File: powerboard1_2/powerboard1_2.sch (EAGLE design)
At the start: 118 parts, among them Q1 IPP80P03P4L04AKSA1, Q2 2N4401TFR, Q3 2N4401TFR, Q4 2N4401TFR, T1 2_POS_TERMINAL, U1 UWE-12/10-Q12PB-C, U2 UWE-5/15-Q12PB-C, U3 UWE-3.3/20-Q12PB-C

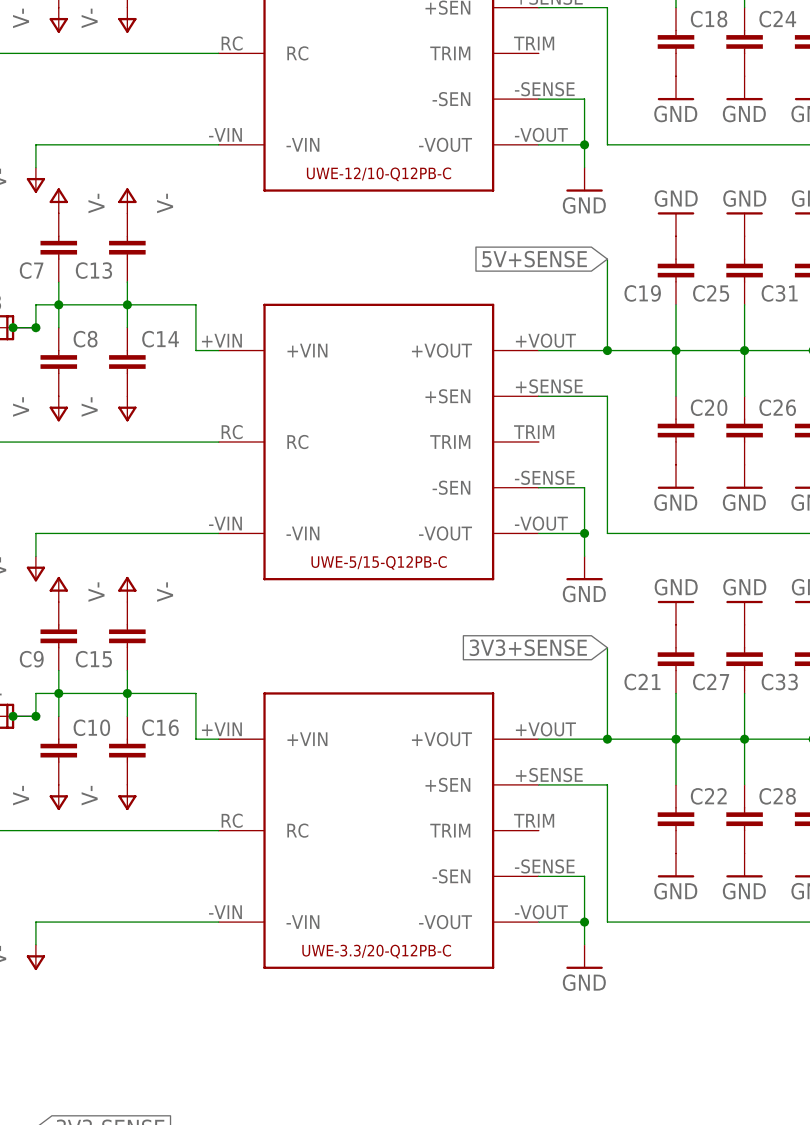
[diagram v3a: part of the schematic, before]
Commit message: Reverted to converters that have input range of 18V to 75V
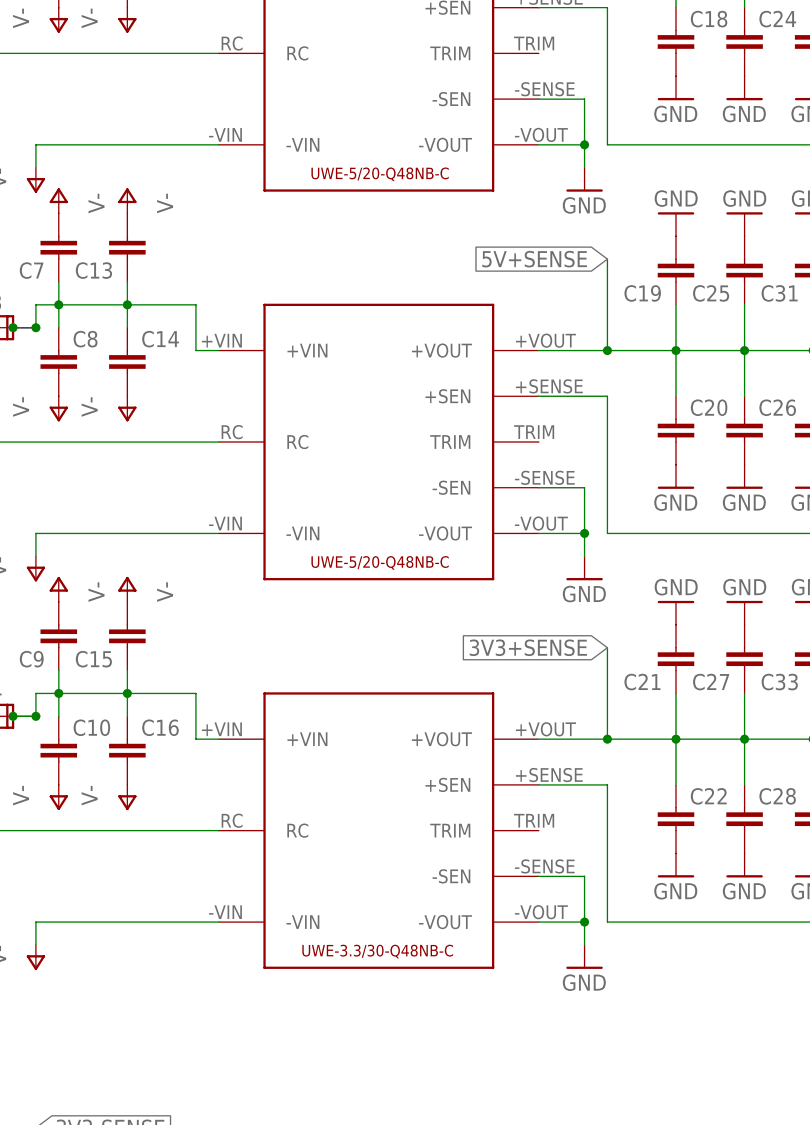
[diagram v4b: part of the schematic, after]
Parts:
- removed U3: UWE-3.3/20-Q12PB-C, New Power Board Library:UWE-3.3/20-Q12PB-C
- added U4: UWE-12/10-Q48NB-C, New Power Board Library:UWE-12/10-Q48NB-C
- U1: value UWE-12/10-Q12PB-C -> UWE-5/20-Q48NB-C; device New Power Board Library:UWE-12/10-Q12PB-C -> New Power Board Library:UWE-5/20-Q48NB-C
- U2: value UWE-5/15-Q12PB-C -> UWE-3.3/30-Q48NB-C; device New Power Board Library:UWE-5/15-Q12PB-C -> New Power Board Library:UWE-3.3/30-Q48NB-C
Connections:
- net 12V+SENSE: now also U4.+VOUT; no longer U1.+VOUT
- net 12V-SENSE: now also U4.+SEN; no longer U1.+SEN
- net 3V3+SENSE: now also U2.+VOUT; no longer U3.+VOUT
- net 3V3-SENSE: now also U2.+SEN; no longer U3.+SEN
- net 5V+SENSE: now also U1.+VOUT; no longer U2.+VOUT
- net 5V-SENSE: now also U1.+SEN; no longer U2.+SEN
- net ENABLE_12V: now also U4.RC; no longer U1.RC
- net ENABLE_3V3: now also U2.RC; no longer U3.RC
- net ENABLE_5V: now also U1.RC; no longer U2.RC
- net GND: now also U4.-SEN, U4.-VOUT; no longer U3.-SEN, U3.-VOUT
- net N$12: now also U2.+VIN; no longer U3.+VIN
- net N$5: now also U4.+VIN; no longer U1.+VIN
- net N$7: now also U1.+VIN; no longer U2.+VIN
- net V-: now also U4.-VIN; no longer U3.-VIN
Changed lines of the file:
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@@
 <?xml version="1.0" encoding="utf-8"?>
 <!DOCTYPE eagle SYSTEM "eagle.dtd">
-<eagle version="8.1.1">
+<eagle version="8.2.0">
 <drawing>
 <settings>
@@
 <part name="GND13" library="supply1" deviceset="GND" device=""/>
 <part name="GND7" library="supply1" deviceset="GND" device=""/>
-<part name="U1" library="New Power Board Library" deviceset="UWE-12/10-Q12PB-C" device=""/>
-<part name="U2" library="New Power Board Library" deviceset="UWE-5/15-Q12PB-C" device=""/>
-<part name="U3" library="New Power Board Library" deviceset="UWE-3.3/20-Q12PB-C" device=""/>
 <part name="JP9" library="pinhead" deviceset="PINHD-1X2" device="/90"/>
 <part name="JP8" library="pinhead" deviceset="PINHD-2X3" device="/90"/>
@@
 <part name="R19" library="resistor" deviceset="R-US_" device="0204/7" value="36k"/>
 <part name="GND26" library="supply1" deviceset="GND" device=""/>
+<part name="U4" library="New Power Board Library" deviceset="UWE-12/10-Q48NB-C" device=""/>
+<part name="U1" library="New Power Board Library" deviceset="UWE-5/20-Q48NB-C" device=""/>
+<part name="U2" library="New Power Board Library" deviceset="UWE-3.3/30-Q48NB-C" device=""/>
 </parts>
 <sheets>
@@
 <instance part="GND13" gate="1" x="177.8" y="256.54" rot="R180"/>
 <instance part="GND7" gate="1" x="170.18" y="256.54" rot="R180"/>
-<instance part="U1" gate="G$1" x="137.16" y="231.14"/>
-<instance part="U2" gate="G$1" x="137.16" y="187.96"/>
-<instance part="U3" gate="G$1" x="137.16" y="144.78"/>
 <instance part="JP9" gate="G$1" x="55.88" y="144.78" rot="MR0"/>
 <instance part="JP8" gate="A" x="45.72" y="167.64" rot="MR0"/>
@@
 <instance part="R19" gate="G$1" x="251.46" y="137.16" rot="R90"/>
 <instance part="GND26" gate="1" x="238.76" y="111.76"/>
+<instance part="U4" gate="G$1" x="137.16" y="231.14"/>
+<instance part="U1" gate="G$1" x="137.16" y="187.96"/>
+<instance part="U2" gate="G$1" x="137.16" y="144.78"/>
 </instances>
 <busses>
@@
 <wire x1="99.06" y1="218.44" x2="99.06" y2="220.98" width="0.1524" layer="91"/>
 <wire x1="99.06" y1="220.98" x2="119.38" y2="220.98" width="0.1524" layer="91"/>
-<pinref part="U1" gate="G$1" pin="-VIN"/>
+<pinref part="U4" gate="G$1" pin="-VIN"/>
 </segment>
 <segment>
@@
 <wire x1="99.06" y1="132.08" x2="99.06" y2="134.62" width="0.1524" layer="91"/>
 <wire x1="99.06" y1="134.62" x2="119.38" y2="134.62" width="0.1524" layer="91"/>
-<pinref part="U3" gate="G$1" pin="-VIN"/>
+<pinref part="U2" gate="G$1" pin="-VIN"/>
 </segment>
 <segment>
@@
 <wire x1="99.06" y1="175.26" x2="99.06" y2="177.8" width="0.1524" layer="91"/>
 <wire x1="99.06" y1="177.8" x2="119.38" y2="177.8" width="0.1524" layer="91"/>
-<pinref part="U2" gate="G$1" pin="-VIN"/>
+<pinref part="U1" gate="G$1" pin="-VIN"/>
 </segment>
 <segment>
@@
 <wire x1="154.94" y1="134.62" x2="160.02" y2="134.62" width="0.1524" layer="91"/>
 <junction x="160.02" y="134.62"/>
-<pinref part="U3" gate="G$1" pin="-SEN"/>
-<pinref part="U3" gate="G$1" pin="-VOUT"/>
+<pinref part="U2" gate="G$1" pin="-SEN"/>
+<pinref part="U2" gate="G$1" pin="-VOUT"/>
 </segment>
 <segment>
@@
 <wire x1="154.94" y1="177.8" x2="160.02" y2="177.8" width="0.1524" layer="91"/>
 <junction x="160.02" y="177.8"/>
-<pinref part="U2" gate="G$1" pin="-SEN"/>
-<pinref part="U2" gate="G$1" pin="-VOUT"/>
+<pinref part="U1" gate="G$1" pin="-SEN"/>
+<pinref part="U1" gate="G$1" pin="-VOUT"/>
 </segment>
 <segment>
@@
 <wire x1="160.02" y1="226.06" x2="160.02" y2="220.98" width="0.1524" layer="91"/>
 <junction x="160.02" y="220.98"/>
-<pinref part="U1" gate="G$1" pin="-SEN"/>
-<pinref part="U1" gate="G$1" pin="-VOUT"/>
+<pinref part="U4" gate="G$1" pin="-SEN"/>
+<pinref part="U4" gate="G$1" pin="-VOUT"/>
 </segment>
 <segment>
@@
 <wire x1="162.56" y1="251.46" x2="162.56" y2="241.3" width="0.1524" layer="91"/>
 <junction x="162.56" y="241.3"/>
-<pinref part="U1" gate="G$1" pin="+VOUT"/>
+<pinref part="U4" gate="G$1" pin="+VOUT"/>
 </segment>
 <segment>
@@
 <label x="162.56" y="208.28" size="1.778" layer="95" rot="R180" xref="yes"/>
 <wire x1="162.56" y1="208.28" x2="162.56" y2="198.12" width="0.1524" layer="91"/>
-<pinref part="U2" gate="G$1" pin="+VOUT"/>
+<pinref part="U1" gate="G$1" pin="+VOUT"/>
 </segment>
 <segment>
@@
 <label x="162.56" y="165.1" size="1.778" layer="95" rot="R180" xref="yes"/>
 <wire x1="162.56" y1="165.1" x2="162.56" y2="154.94" width="0.1524" layer="91"/>
-<pinref part="U3" gate="G$1" pin="+VOUT"/>
+<pinref part="U2" gate="G$1" pin="+VOUT"/>
 </segment>
 <segment>
@@
 <junction x="101.6" y="246.38"/>
 <junction x="109.22" y="246.38"/>
-<pinref part="U1" gate="G$1" pin="+VIN"/>
+<pinref part="U4" gate="G$1" pin="+VIN"/>
 </segment>
 </net>
@@
 <wire x1="200.66" y1="243.84" x2="200.66" y2="241.3" width="0.1524" layer="91"/>
 <junction x="200.66" y="241.3"/>
-<pinref part="U1" gate="G$1" pin="+SEN"/>
+<pinref part="U4" gate="G$1" pin="+SEN"/>
 </segment>
 <segment>
@@
 <junction x="200.66" y="198.12"/>
 <label x="200.66" y="200.66" size="1.778" layer="95" rot="R90" xref="yes"/>
-<pinref part="U2" gate="G$1" pin="+SEN"/>
+<pinref part="U1" gate="G$1" pin="+SEN"/>
 </segment>
 <segment>
@@
 <junction x="200.66" y="154.94"/>
 <label x="200.66" y="157.48" size="1.778" layer="95" rot="R90" xref="yes"/>
-<pinref part="U3" gate="G$1" pin="+SEN"/>
+<pinref part="U2" gate="G$1" pin="+SEN"/>
 </segment>
 <segment>
@@
 <wire x1="91.44" y1="228.6" x2="91.44" y2="231.14" width="0.1524" layer="91"/>
 <wire x1="91.44" y1="231.14" x2="119.38" y2="231.14" width="0.1524" layer="91"/>
-<pinref part="U1" gate="G$1" pin="RC"/>
+<pinref part="U4" gate="G$1" pin="RC"/>
 </segment>
 </net>
@@
 <wire x1="91.44" y1="185.42" x2="91.44" y2="187.96" width="0.1524" layer="91"/>
 <wire x1="91.44" y1="187.96" x2="119.38" y2="187.96" width="0.1524" layer="91"/>
-<pinref part="U2" gate="G$1" pin="RC"/>
+<pinref part="U1" gate="G$1" pin="RC"/>
 </segment>
 </net>
@@
 <wire x1="91.44" y1="142.24" x2="91.44" y2="144.78" width="0.1524" layer="91"/>
 <wire x1="91.44" y1="144.78" x2="119.38" y2="144.78" width="0.1524" layer="91"/>
-<pinref part="U3" gate="G$1" pin="RC"/>
+<pinref part="U2" gate="G$1" pin="RC"/>
 </segment>
 </net>
@@
 <wire x1="116.84" y1="198.12" x2="119.38" y2="198.12" width="0.1524" layer="91"/>
 <junction x="99.06" y="200.66"/>
-<pinref part="U2" gate="G$1" pin="+VIN"/>
+<pinref part="U1" gate="G$1" pin="+VIN"/>
 </segment>
 </net>
@@
 <junction x="109.22" y="160.02"/>
 <junction x="99.06" y="157.48"/>
-<pinref part="U3" gate="G$1" pin="+VIN"/>
 <wire x1="116.84" y1="154.94" x2="119.38" y2="154.94" width="0.1524" layer="91"/>
-</segment>
-</net>
+<pinref part="U2" gate="G$1" pin="+VIN"/>
+</segment>
+</net>
